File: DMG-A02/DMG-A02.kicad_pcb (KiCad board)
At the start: 2 copper layers, 51 x 60.7 mm, 19 parts, among them U0 CartBus, U1 SSOP-32_MROM, U2 LQFP-32_MBC, U3 SOIC-28_SRAM, U4 SO-8_SYSRST

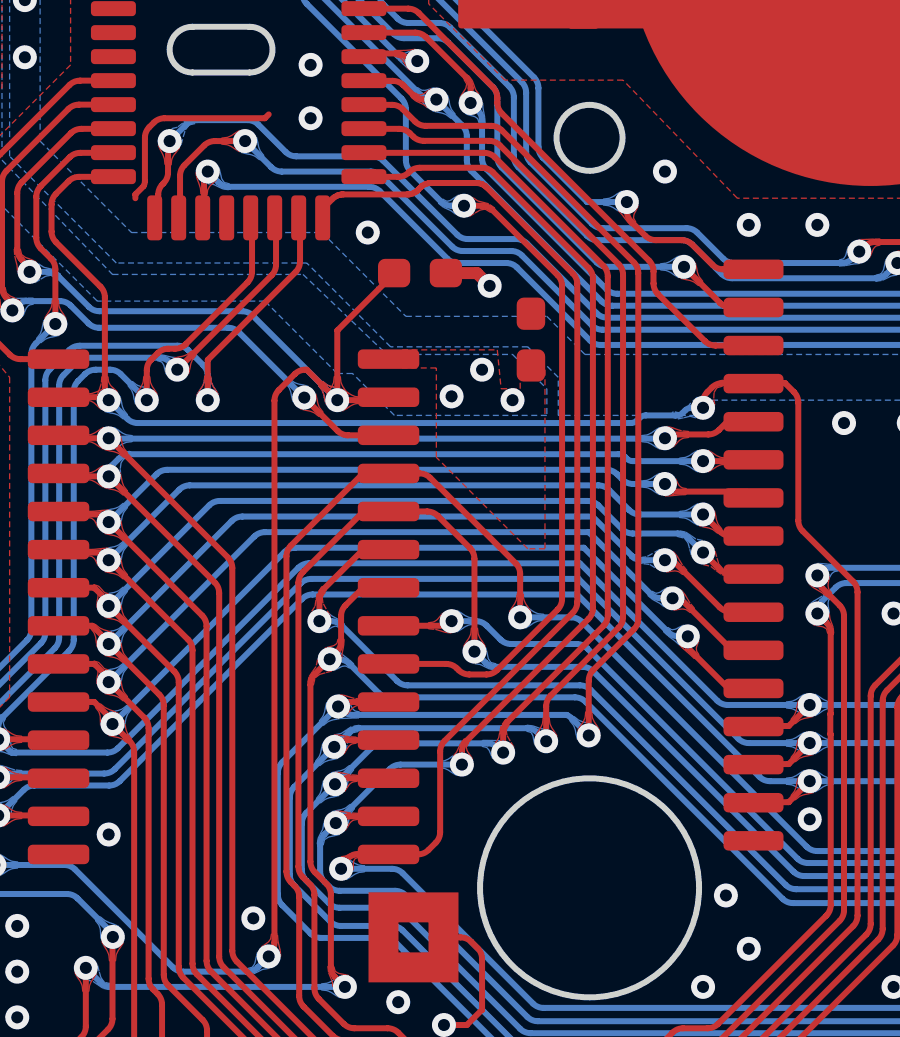
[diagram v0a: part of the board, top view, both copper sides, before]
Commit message: Fix D3 arc issue
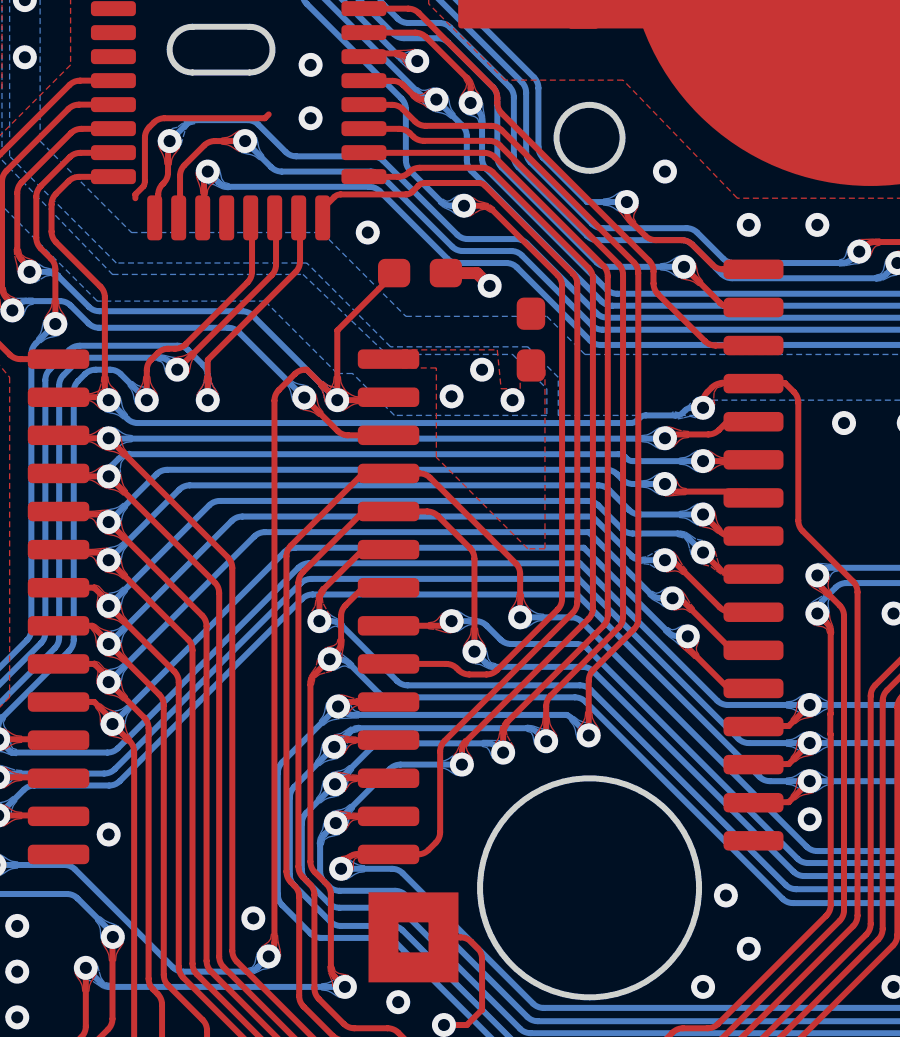
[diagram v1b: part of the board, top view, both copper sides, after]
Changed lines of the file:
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@@
     (fp_arc (start -24.95 -8.8) (mid -24.773243 -8.726796) (end -24.7 -8.550056) (layer "F.Fab") (width 0.05))
     (fp_arc (start -23.2 0) (mid -24.26066 -0.43934) (end -24.7 -1.5) (layer "F.Fab") (width 0.05))
-    (fp_arc (start 24.7 -8.550056) (mid 24.773194 -8.726806) (end 24.949944 -8.800056) (layer "F.Fab") (width 0.05))
+    (fp_arc (start 24.7 -8.550056) (mid 24.773188 -8.726841) (end 24.949944 -8.800056) (layer "F.Fab") (width 0.05))
     (fp_arc (start 25.5 -9.3) (mid 25.353553 -8.946447) (end 25 -8.8) (layer "F.Fab") (width 0.05))
     (pad "1" thru_hole circle locked (at -23.5 -7.6) (size 0.8 0.8) (drill 0.6) (layers *.Cu *.Mask)
@@
   (arc (start 149.113385 98.18952) (mid 149.304726 98.15146) (end 149.466938 98.043074) (width 0.2) (layer "B.Cu") (net 25))
   (segment (start 157.050465 100.632535) (end 156.845 100.838) (width 0.2) (layer "F.Cu") (net 26))
-  (segment (start 159.758578 100.337422) (end 160.000554 100.095446) (width 0.2) (layer "F.Cu") (net 26))
-  (segment (start 159.492553 78.251447) (end 159.404446 78.339554) (width 0.2) (layer "F.Cu") (net 26))
-  (segment (start 160.293447 96.704109) (end 164.572554 92.425002) (width 0.2) (layer "F.Cu") (net 26))
-  (segment (start 159.540009 78.206086) (end 159.492553 78.251447) (width 0.2) (layer "F.Cu") (net 26))
-  (segment (start 159.356849 78.38473) (end 159.243225 78.450331) (width 0.2) (layer "F.Cu") (net 26))
   (segment (start 156.845 100.838) (end 156.845 100.965) (width 0.2) (layer "F.Cu") (net 26))
   (segment (start 158.426447 100.486088) (end 157.404019 100.486088) (width 0.2) (layer "F.Cu") (net 26))
-  (segment (start 157.533238 100.483869) (end 159.405024 100.483869) (width 0.2) (layer "F.Cu") (net 26))
-  (segment (start 156.55977 78.632447) (end 156.231145 78.961072) (width 0.2) (layer "F.Cu") (net 26))
-  (segment (start 156.720903 78.521454) (end 156.607226 78.587086) (width 0.2) (layer "F.Cu") (net 26))
-  (segment (start 161.347059 78.105) (end 159.846107 78.105) (width 0.2) (layer "F.Cu") (net 26))
+  (segment (start 156.231145 78.961072) (end 156.618349 78.573868) (width 0.2) (layer "F.Cu") (net 26))
+  (segment (start 161.642714 78.192868) (end 164.572553 81.122707) (width 0.2) (layer "F.Cu") (net 26))
+  (segment (start 160.147 97.057663) (end 160.147 99.741893) (width 0.2) (layer "F.Cu") (net 26))
   (segment (start 181.878316 100.014791) (end 184.068298 100.014791) (width 0.2) (layer "F.Cu") (net 26))
   (segment (start 179.003317 106.285576) (end 179.003317 102.88979) (width 0.2) (layer "F.Cu") (net 26))
-  (segment (start 161.539391 78.140669) (end 161.41266 78.106712) (width 0.2) (layer "F.Cu") (net 26))
-  (segment (start 164.719 92.071449) (end 164.719 81.476941) (width 0.2) (layer "F.Cu") (net 26))
-  (segment (start 159.780476 78.106481) (end 159.653686 78.140454) (width 0.2) (layer "F.Cu") (net 26))
   (segment (start 177.877 109.65) (end 177.877 107.826107) (width 0.2) (layer "F.Cu") (net 26))
-  (segment (start 161.700612 78.251446) (end 161.653015 78.20627) (width 0.2) (layer "F.Cu") (net 26))
-  (segment (start 156.607226 78.587086) (end 156.55977 78.632447) (width 0.2) (layer "F.Cu") (net 26))
-  (segment (start 159.846107 78.105) (end 159.780476 78.106481) (width 0.2) (layer "F.Cu") (net 26))
-  (segment (start 160.147 99.741893) (end 160.147 97.057663) (width 0.2) (layer "F.Cu") (net 26))
-  (segment (start 159.243225 78.450331) (end 159.116494 78.484288) (width 0.2) (layer "F.Cu") (net 26))
-  (segment (start 161.41266 78.106712) (end 161.347059 78.105) (width 0.2) (layer "F.Cu") (net 26))
-  (segment (start 159.116494 78.484288) (end 159.050893 78.486) (width 0.2) (layer "F.Cu") (net 26))
-  (segment (start 159.404446 78.339554) (end 159.356849 78.38473) (width 0.2) (layer "F.Cu") (net 26))
+  (segment (start 160.000554 100.095446) (end 159.758578 100.337422) (width 0.2) (layer "F.Cu") (net 26))
+  (segment (start 159.636264 78.105) (end 161.430582 78.105) (width 0.2) (layer "F.Cu") (net 26))
+  (segment (start 159.218868 78.398132) (end 159.424132 78.192868) (width 0.2) (layer "F.Cu") (net 26))
   (segment (start 178.023447 107.472553) (end 178.856871 106.639129) (width 0.2) (layer "F.Cu") (net 26))
   (segment (start 179.324 102.362) (end 181.524763 100.161237) (width 0.2) (layer "F.Cu") (net 26))
+  (segment (start 164.572554 92.425002) (end 160.293447 96.704109) (width 0.2) (layer "F.Cu") (net 26))
   (segment (start 179.149764 102.536236) (end 179.324 102.362) (width 0.2) (layer "F.Cu") (net 26))
-  (segment (start 161.653015 78.20627) (end 161.539391 78.140669) (width 0.2) (layer "F.Cu") (net 26))
-  (segment (start 164.572553 81.123387) (end 161.700612 78.251446) (width 0.2) (layer "F.Cu") (net 26))
-  (segment (start 159.050893 78.486) (end 156.913324 78.486) (width 0.2) (layer "F.Cu") (net 26))
-  (segment (start 156.847693 78.487481) (end 156.720903 78.521454) (width 0.2) (layer "F.Cu") (net 26))
-  (segment (start 159.653686 78.140454) (end 159.540009 78.206086) (width 0.2) (layer "F.Cu") (net 26))
-  (segment (start 156.913324 78.486) (end 156.847693 78.487481) (width 0.2) (layer "F.Cu") (net 26))
+  (segment (start 156.830481 78.486) (end 159.006736 78.486) (width 0.2) (layer "F.Cu") (net 26))
+  (segment (start 159.405024 100.483869) (end 157.533238 100.483869) (width 0.2) (layer "F.Cu") (net 26))
+  (segment (start 164.719 81.476941) (end 164.719 92.071449) (width 0.2) (layer "F.Cu") (net 26))
+  (segment (start 164.572553 81.122707) (end 164.572553 81.123387) (width 0.2) (layer "F.Cu") (net 26))
   (via (at 179.324 102.362) (size 0.8) (drill 0.4) (layers "F.Cu" "B.Cu") (free) (net 26))
   (via (at 156.845 100.965) (size 0.8) (drill 0.4) (layers "F.Cu" "B.Cu") (free) (net 26))
   (arc (start 179.003317 106.285576) (mid 178.965257 106.476917) (end 178.856871 106.639129) (width 0.2) (layer "F.Cu") (net 26))
-  (arc (start 159.758578 100.337422) (mid 159.596366 100.445809) (end 159.405024 100.483869) (width 0.2) (layer "F.Cu") (net 26))
-  (arc (start 164.719 92.071449) (mid 164.68094 92.26279) (end 164.572554 92.425002) (width 0.2) (layer "F.Cu") (net 26))
+  (arc (start 160.293447 96.704109) (mid 160.18506 96.866321) (end 160.147 97.057663) (width 0.2) (layer "F.Cu") (net 26))
+  (arc (start 161.430582 78.105) (mid 161.545387 78.127836) (end 161.642714 78.192868) (width 0.2) (layer "F.Cu") (net 26))
   (arc (start 177.877 107.826107) (mid 177.91506 107.634765) (end 178.023447 107.472553) (width 0.2) (layer "F.Cu") (net 26))
-  (arc (start 160.293447 96.704109) (mid 160.18506 96.866321) (end 160.147 97.057663) (width 0.2) (layer "F.Cu") (net 26))
   (arc (start 181.878316 100.014791) (mid 181.686975 100.052851) (end 181.524763 100.161237) (width 0.2) (layer "F.Cu") (net 26))
   (arc (start 157.404019 100.486088) (mid 157.212677 100.524148) (end 157.050465 100.632535) (width 0.2) (layer "F.Cu") (net 26))
-  (arc (start 164.719 81.476941) (mid 164.68094 81.285599) (end 164.572553 81.123387) (width 0.2) (layer "F.Cu") (net 26))
+  (arc (start 156.618349 78.573868) (mid 156.715676 78.508836) (end 156.830481 78.486) (width 0.2) (layer "F.Cu") (net 26))
+  (arc (start 159.006736 78.486) (mid 159.121541 78.463164) (end 159.218868 78.398132) (width 0.2) (layer "F.Cu") (net 26))
   (arc (start 179.003317 102.88979) (mid 179.041377 102.698448) (end 179.149764 102.536236) (width 0.2) (layer "F.Cu") (net 26))
-  (arc (start 160.000554 100.095446) (mid 160.10894 99.933234) (end 160.147 99.741893) (width 0.2) (layer "F.Cu") (net 26))
+  (arc (start 164.572553 81.123387) (mid 164.680941 81.285602) (end 164.719 81.476941) (width 0.2) (layer "F.Cu") (net 26))
+  (arc (start 160.147 99.741893) (mid 160.10894 99.933234) (end 160.000554 100.095446) (width 0.2) (layer "F.Cu") (net 26))
+  (arc (start 164.719 92.071449) (mid 164.68094 92.26279) (end 164.572554 92.425002) (width 0.2) (layer "F.Cu") (net 26))
+  (arc (start 159.758578 100.337422) (mid 159.596366 100.445809) (end 159.405024 100.483869) (width 0.2) (layer "F.Cu") (net 26))
+  (arc (start 159.424132 78.192868) (mid 159.521459 78.127836) (end 159.636264 78.105) (width 0.2) (layer "F.Cu") (net 26))
   (segment (start 179.177553 104.667447) (end 178.389935 105.455065) (width 0.2) (layer "B.Cu") (net 26))
   (segment (start 163.240064 105.455064) (end 158.896446 101.111446) (width 0.2) (layer "B.Cu") (net 26))

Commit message: Update timestamp.
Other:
- board text added: "RDM 2023MAR"
- board text removed: "RDM 2023FEB"
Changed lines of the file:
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@@
     (fp_arc (start -24.95 -8.8) (mid -24.773243 -8.726796) (end -24.7 -8.550056) (layer "F.Fab") (width 0.05))
     (fp_arc (start -23.2 0) (mid -24.26066 -0.43934) (end -24.7 -1.5) (layer "F.Fab") (width 0.05))
-    (fp_arc (start 24.7 -8.550056) (mid 24.773188 -8.726841) (end 24.949944 -8.800056) (layer "F.Fab") (width 0.05))
+    (fp_arc (start 24.7 -8.550056) (mid 24.773194 -8.726806) (end 24.949944 -8.800056) (layer "F.Fab") (width 0.05))
     (fp_arc (start 25.5 -9.3) (mid 25.353553 -8.946447) (end 25 -8.8) (layer "F.Fab") (width 0.05))
     (pad "1" thru_hole circle locked (at -23.5 -7.6) (size 0.8 0.8) (drill 0.6) (layers *.Cu *.Mask)
@@
     (effects (font (size 1 1) (thickness 0.15)) (justify mirror))
   )
-  (gr_text "RDM 2023FEB" (at 188.214 68.072 90) (layer "B.Mask")
+  (gr_text "RDM 2023MAR" (at 188.214 68.072 90) (layer "B.Mask")
     (effects (font (size 0.75 0.75) (thickness 0.1)) (justify mirror))
   )
@@
     )
   )
+  (zone (net 0) (net_name "") (layer "B.Cu") (hatch edge 0.508)
+    (connect_pads (clearance 0))
+    (min_thickness 0.254)
+    (keepout (tracks allowed) (vias allowed) (pads allowed) (copperpour not_allowed) (footprints allowed))
+    (fill (thermal_gap 0.508) (thermal_bridge_width 0.508))
+    (polygon
+      (pts
+        (xy 179.563247 72.365295)
+        (xy 179.52382 72.167083)
+        (xy 179.411542 71.999048)
+        (xy 179.243507 71.88677)
+        (xy 179.045295 71.847343)
+        (xy 178.847083 71.88677)
+        (xy 178.679048 71.999048)
+        (xy 178.56677 72.167083)
+        (xy 178.527343 72.365295)
+        (xy 178.56677 72.563507)
+        (xy 178.679048 72.731542)
+        (xy 178.847083 72.84382)
+        (xy 179.045295 72.883247)
+        (xy 179.243507 72.84382)
+        (xy 179.411542 72.731542)
+        (xy 179.52382 72.563507)
+      )
+    )
+  )
   (zone (net 12) (net_name "A05") (layer "B.Cu") (hatch edge 0.508)
     (priority 16962)
@@
     )
   )
+  (zone (net 0) (net_name "") (layer "B.Cu") (hatch edge 0.508)
+    (connect_pads (clearance 0))
+    (min_thickness 0.254)
+    (keepout (tracks allowed) (vias allowed) (pads allowed) (copperpour not_allowed) (footprints allowed))
+    (fill (thermal_gap 0.508) (thermal_bridge_width 0.508))
+    (polygon
+      (pts
+        (xy 176.149 64.135)
+        (xy 176.109573 63.936788)
+        (xy 175.997295 63.768753)
+        (xy 175.82926 63.656475)
+        (xy 175.631048 63.617048)
+        (xy 175.432836 63.656475)
+        (xy 175.264801 63.768753)
+        (xy 175.152523 63.936788)
+        (xy 175.113096 64.135)
+        (xy 175.152523 64.333212)
+        (xy 175.264801 64.501247)
+        (xy 175.432836 64.613525)
+        (xy 175.631048 64.652952)
+        (xy 175.82926 64.613525)
+        (xy 175.997295 64.501247)
+        (xy 176.109573 64.333212)
+      )
+    )
+  )
   (zone (net 19) (net_name "A12") (layer "B.Cu") (hatch edge 0.508)
     (priority 16962)
@@
     )
   )
+  (zone (net 0) (net_name "") (layer "B.Cu") (hatch edge 0.508)
+    (connect_pads (clearance 0))
+    (min_thickness 0.254)
+    (keepout (tracks allowed) (vias allowed) (pads allowed) (copperpour not_allowed) (footprints allowed))
+    (fill (thermal_gap 0.508) (thermal_bridge_width 0.508))
+    (polygon
+      (pts
+        (xy 176.163753 71.017705)
+        (xy 176.124326 70.819493)
+        (xy 176.012048 70.651458)
+        (xy 175.844013 70.53918)
+        (xy 175.645801 70.499753)
+        (xy 175.447589 70.53918)
+        (xy 175.279554 70.651458)
+        (xy 175.167276 70.819493)
+        (xy 175.127849 71.017705)
+        (xy 175.167276 71.215917)
+        (xy 175.279554 71.383952)
+        (xy 175.447589 71.49623)
+        (xy 175.645801 71.535657)
+        (xy 175.844013 71.49623)
+        (xy 176.012048 71.383952)
+        (xy 176.124326 71.215917)
+      )
+    )
+  )
   (zone (net 27) (net_name "D4") (layer "B.Cu") (hatch edge 0.508)
     (priority 16962)
@@
     )
   )
+  (zone (net 0) (net_name "") (layer "B.Cu") (hatch edge 0.508)
+    (connect_pads (clearance 0))
+    (min_thickness 0.254)
+    (keepout (tracks allowed) (vias allowed) (pads allowed) (copperpour not_allowed) (footprints allowed))
+    (fill (thermal_gap 0.508) (thermal_bridge_width 0.508))
+    (polygon
+      (pts
+        (xy 176.149 66.929)
+        (xy 176.109573 66.730788)
+        (xy 175.997295 66.562753)
+        (xy 175.82926 66.450475)
+        (xy 175.631048 66.411048)
+        (xy 175.432836 66.450475)
+        (xy 175.264801 66.562753)
+        (xy 175.152523 66.730788)
+        (xy 175.113096 66.929)
+        (xy 175.152523 67.127212)
+        (xy 175.264801 67.295247)
+        (xy 175.432836 67.407525)
+        (xy 175.631048 67.446952)
+        (xy 175.82926 67.407525)
+        (xy 175.997295 67.295247)
+        (xy 176.109573 67.127212)
+      )
+    )
+  )
   (zone (net 37) (net_name "CS_EN") (layer "B.Cu") (hatch edge 0.508)
     (priority 16962)
@@
     )
   )
+  (zone (net 0) (net_name "") (layer "B.Cu") (hatch edge 0.508)
+    (connect_pads (clearance 0))
+    (min_thickness 0.254)
+    (keepout (tracks allowed) (vias allowed) (pads allowed) (copperpour not_allowed) (footprints allowed))
+    (fill (thermal_gap 0.508) (thermal_bridge_width 0.508))
+    (polygon
+      (pts
+        (xy 179.578 70.993)
+        (xy 179.538573 70.794788)
+        (xy 179.426295 70.626753)
+        (xy 179.25826 70.514475)
+        (xy 179.060048 70.475048)
+        (xy 178.861836 70.514475)
+        (xy 178.693801 70.626753)
+        (xy 178.581523 70.794788)
+        (xy 178.542096 70.993)
+        (xy 178.581523 71.191212)
+        (xy 178.693801 71.359247)
+        (xy 178.861836 71.471525)
+        (xy 179.060048 71.510952)
+        (xy 179.25826 71.471525)
+        (xy 179.426295 71.359247)
+        (xy 179.538573 71.191212)
+      )
+    )
+  )
   (zone (net 28) (net_name "D5") (layer "B.Cu") (hatch edge 0.508)
     (priority 16962)
@@
     )
   )
+  (zone (net 0) (net_name "") (layer "B.Cu") (hatch edge 0.508)
+    (connect_pads (clearance 0))
+    (min_thickness 0.254)
+    (keepout (tracks allowed) (vias allowed) (pads allowed) (copperpour not_allowed) (footprints allowed))
+    (fill (thermal_gap 0.508) (thermal_bridge_width 0.508))
+    (polygon
+      (pts
+        (xy 176.163753 65.556705)
+        (xy 176.124326 65.358493)
+        (xy 176.012048 65.190458)
+        (xy 175.844013 65.07818)
+        (xy 175.645801 65.038753)
+        (xy 175.447589 65.07818)
+        (xy 175.279554 65.190458)
+        (xy 175.167276 65.358493)
+        (xy 175.127849 65.556705)
+        (xy 175.167276 65.754917)
+        (xy 175.279554 65.922952)
+        (xy 175.447589 66.03523)
+        (xy 175.645801 66.074657)
+        (xy 175.844013 66.03523)
+        (xy 176.012048 65.922952)
+        (xy 176.124326 65.754917)
+      )
+    )
+  )
   (zone (net 27) (net_name "D4") (layer "B.Cu") (hatch edge 0.508)
     (priority 16962)
@@
     )
   )
+  (zone (net 0) (net_name "") (layer "B.Cu") (hatch edge 0.508)
+    (connect_pads (clearance 0))
+    (min_thickness 0.254)
+    (keepout (tracks allowed) (vias allowed) (pads allowed) (copperpour not_allowed) (footprints allowed))
+    (fill (thermal_gap 0.508) (thermal_bridge_width 0.508))
+    (polygon
+      (pts
+        (xy 176.149 69.596)
+        (xy 176.109573 69.397788)
+        (xy 175.997295 69.229753)
+        (xy 175.82926 69.117475)
+        (xy 175.631048 69.078048)
+        (xy 175.432836 69.117475)
+        (xy 175.264801 69.229753)
+        (xy 175.152523 69.397788)
+        (xy 175.113096 69.596)
+        (xy 175.152523 69.794212)
+        (xy 175.264801 69.962247)
+        (xy 175.432836 70.074525)
+        (xy 175.631048 70.113952)
+        (xy 175.82926 70.074525)
+        (xy 175.997295 69.962247)
+        (xy 176.109573 69.794212)
+      )
+    )
+  )
   (zone (net 24) (net_name "D1") (layer "B.Cu") (hatch edge 0.508)
     (priority 16962)
@@
     )
   )
+  (zone (net 0) (net_name "") (layer "B.Cu") (hatch edge 0.508)
+    (connect_pads (clearance 0))
+    (min_thickness 0.254)
+    (keepout (tracks allowed) (vias allowed) (pads allowed) (copperpour not_allowed) (footprints allowed))
+    (fill (thermal_gap 0.508) (thermal_bridge_width 0.508))
+    (polygon
+      (pts
+        (xy 176.149 72.39)
+        (xy 176.109573 72.191788)
+        (xy 175.997295 72.023753)
+        (xy 175.82926 71.911475)
+        (xy 175.631048 71.872048)
+        (xy 175.432836 71.911475)
+        (xy 175.264801 72.023753)
+        (xy 175.152523 72.191788)
+        (xy 175.113096 72.39)
+        (xy 175.152523 72.588212)
+        (xy 175.264801 72.756247)
+        (xy 175.432836 72.868525)
+        (xy 175.631048 72.907952)
+        (xy 175.82926 72.868525)
+        (xy 175.997295 72.756247)
+        (xy 176.109573 72.588212)
+      )
+    )
+  )
   (zone (net 43) (net_name "RA17") (layer "B.Cu") (hatch edge 0.508)
     (priority 16962)
@@
       )
     )
+  )
+  (zone (net 0) (net_name "") (layer "B.Cu") (hatch edge 0.508)
+    (connect_pads (clearance 0))
+    (min_thickness 0.254)
+    (keepout (tracks allowed) (vias allowed) (pads allowed) (copperpour not_allowed) (footprints allowed))
+    (fill (thermal_gap 0.508) (thermal_bridge_width 0.508))
+    (polygon
+      (pts
+        (xy 179.563247 69.571295)
+        (xy 179.52382 69.373083)
+        (xy 179.411542 69.205048)
+        (xy 179.243507 69.09277)
+        (xy 179.045295 69.053343)
+        (xy 178.847083 69.09277)
+        (xy 178.679048 69.205048)
+        (xy 178.56677 69.373083)
+        (xy 178.527343 69.571295)
+        (xy 178.56677 69.769507)
+        (xy 178.679048 69.937542)
+        (xy 178.847083 70.04982)
+        (xy 179.045295 70.089247)
+        (xy 179.243507 70.04982)
+        (xy 179.411542 69.937542)
+        (xy 179.52382 69.769507)
+      )
+    )
